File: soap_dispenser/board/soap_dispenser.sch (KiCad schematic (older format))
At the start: 43 parts, among them M1 Motor_DC, Q1 PMOS, Q11 NMOS, Q3 PMOS, Q4 NMOS, Q5 NMOS, SW1 SW_SPDT, SW8 SW_Push, U1 ATtiny48-AU

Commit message: Updated schema and capture files.
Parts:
- added C11, C18: C_Small, symbol Device:C_Small
- added RN7A, RN7B: 1M, symbol Device:R_Small_US
- added TP7: TestPoint, symbol Connector:TestPoint
- renumbered Q5 to Q2
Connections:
- net +6V: now also RN7A.1
- net CURRENT1: now also TP7.1
- net GNDD: now also C11.1, C18.1, RN7B.2
- net VSENSE: now reaches U1.19 (PA0)
- net VSENSE: now also J?.4 (Pin_4), C11.2, RN7A.2, RN7B.1
- net at Q?.2 (G), R23.2, R26.1: now also C18.2
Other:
- note added: "L-0"
- note added: "L-1"
- note added: "L-2"
- note added: "L-3"
- note added: "L-4"
- note added: "L-5"
- note added: "L-6"
- note added: "L-7"
- moved on the sheet: D4A, D4B, RN5A, RN5B, TP20, TP21

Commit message: Minor schema cleanup
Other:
- note added: "TODO: determine state of unconnected\npins (for minimal current)"
- moved on the sheet: C11, C?, D4A, D4B, R30, R9, RN5A, RN5B, RN6B?, RN7A, RN7B, SW1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

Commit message: First working version. Still a bunch of TODOs.
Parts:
- removed Q11, Q5, Q?: NMOS, symbol Device:Q_NMOS_DGS
- added Q11, Q5, Q?: MMBT4401, symbol Device:Q_NPN_BCE
- D4B: value YELLOW -> GREEN
- Q1, Q3: value PMOS -> DMG2305UX
- Q2, Q4: value NMOS -> DMG3420U
- renumbered C18 to C18_DNP
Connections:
- net CURRENT2: now also Q?.2 (C)
- net GNDD: now also Q11.3 (E), Q5.3 (E), Q?.3 (E)
- net at Q3.2 (G), RN6B.2: now also Q11.2 (C)
- net at Q1.2 (G), RN6A.2: now also Q5.2 (C)
- net at R5.1, R6.2: now also Q5.1 (B)
- net at R10.2, R10.2: now also Q11.1 (B)
- net at C18_DNP.2, R23.2, R26.1: now also Q?.1 (B)
- net #YELLOW renamed #GREEN
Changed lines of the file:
@@
 P 8350 2450
 F 0 "Q2" H 8556 2496 50  0000 L CNN
-F 1 "NMOS" H 7900 2600 50  0001 L CNN
+F 1 "DMG3420U" H 7900 2550 50  0000 L CNN
 F 2 "" H 8550 2550 50  0001 C CNN
 F 3 "~" H 8350 2450 50  0001 C CNN
@@
 P 6750 1550
 F 0 "Q3" H 6650 1400 50  0000 L CNN
-F 1 "PMOS" H 6950 1550 50  0001 L CNN
+F 1 "DMG2305UX" H 6950 1450 50  0000 L CNN
 F 2 "" H 6950 1650 50  0001 C CNN
 F 3 "~" H 6750 1550 50  0001 C CNN
@@
 	8550 1550 8750 1550
 $Comp
-L Device:Q_NMOS_DGS Q5
-U 1 1 5C0E3D5E
-P 8850 1800
-F 0 "Q5" H 9056 1846 50  0000 L CNN
-F 1 "NMOS" H 8400 1950 50  0001 L CNN
-F 2 "" H 9050 1900 50  0001 C CNN
-F 3 "~" H 8850 1800 50  0001 C CNN
-	1    8850 1800
-	-1   0    0    -1
-$EndComp
-$Comp
-L Device:Q_NMOS_DGS Q11
-U 1 1 5C0E41F9
-P 6250 1800
-F 0 "Q11" H 6456 1846 50  0000 L CNN
-F 1 "NMOS" H 6450 1750 50  0001 L CNN
-F 2 "" H 6450 1900 50  0001 C CNN
-F 3 "~" H 6250 1800 50  0001 C CNN
-	1    6250 1800
-	1    0    0    -1
-$EndComp
-$Comp
 L Device:R_Small_US R10
 U 1 1 5C0E4F52
@@
 P 8350 1550
 F 0 "Q1" H 8200 1400 50  0000 L CNN
-F 1 "PMOS" H 8556 1595 50  0001 L CNN
+F 1 "DMG2305UX" H 8500 1350 50  0000 L CNN
 F 2 "Package_TO_SOT_THT:TO-92_Inline" H 8550 1475 50  0001 L CIN
 F 3 "http://www.vishay.com/docs/70209/70209.pdf" H 8350 1550 50  0001 L CNN
@@
 U 1 1 5C0EEC8E
 P 6750 2450
-F 0 "Q4" H 6955 2450 50  0000 L CNN
-F 1 "NMOS" H 6955 2405 50  0001 L CNN
+F 0 "Q4" H 6950 2500 50  0000 L CNN
+F 1 "DMG3420U" H 6950 2400 50  0000 L CNN
 F 2 "" H 6950 2550 50  0001 C CNN
-F 3 "~" H 6750 2450 50  0001 C CNN
+F 3 "" H 6750 2450 50  0001 C CNN
 	1    6750 2450
 	1    0    0    -1
@@
 #RED
 Text GLabel 5050 5950 3    50   Input ~ 0
-#YELLOW
+#GREEN
 Text GLabel 2900 4650 2    50   Output ~ 0
 #RED
 Text GLabel 2900 4750 2    50   Output ~ 0
-#YELLOW
+#GREEN
 Wire Wire Line
 	2550 4650 2900 4650
@@
 P 5050 5300
 F 0 "D4B" V 5150 5200 50  0000 R CNN
-F 1 "YELLOW" V 5050 5200 50  0000 R CNN
+F 1 "GREEN" V 5050 5200 50  0000 R CNN
 F 2 "" H 5050 5300 50  0001 C CNN
 F 3 "~" H 5050 5300 50  0001 C CNN
@@
 	4150 7150 5650 7150
 $Comp
-L Device:Q_NMOS_DGS Q?
-U 1 1 5C1076F9
-P 8550 3600
-F 0 "Q?" H 8756 3646 50  0000 L CNN
-F 1 "NMOS" H 8100 3750 50  0001 L CNN
-F 2 "" H 8750 3700 50  0001 C CNN
-F 3 "~" H 8550 3600 50  0001 C CNN
-	1    8550 3600
-	1    0    0    -1
-$EndComp
-$Comp
 L Device:R_Small_US R19
 U 1 1 5C10B5B4
@@
 	7300 3600 7150 3600
 $Comp
-L Device:C_Small C18
+L Device:C_Small C18_DNP
 U 1 1 5C146FA6
 P 8000 3750
-F 0 "C18" H 7850 3850 50  0000 C CNN
+F 0 "C18_DNP" H 7800 3850 50  0000 C CNN
 F 1 "C_Small" V 8200 3800 50  0001 C CNN
 F 2 "" H 8000 3750 50  0001 C CNN
@@
 Wire Wire Line
 	8500 5300 8500 5400
+$Comp
+L Device:Q_NPN_BCE Q11
+U 1 1 5C137253
+P 6250 1800
+F 0 "Q11" H 6441 1846 50  0000 L CNN
+F 1 "MMBT4401" H 6441 1755 50  0000 L CNN
+F 2 "" H 6450 1900 50  0001 C CNN
+F 3 "~" H 6250 1800 50  0001 C CNN
+	1    6250 1800
+	1    0    0    -1
+$EndComp
+$Comp
+L Device:Q_NPN_BCE Q5
+U 1 1 5C1430B6
+P 8850 1800
+F 0 "Q5" H 9040 1846 50  0000 L CNN
+F 1 "MMBT4401" H 8500 2000 50  0000 L CNN
+F 2 "" H 9050 1900 50  0001 C CNN
+F 3 "" H 8850 1800 50  0001 C CNN
+	1    8850 1800
+	-1   0    0    -1
+$EndComp
+$Comp
+L Device:Q_NPN_BCE Q?
+U 1 1 5C155532
+P 8550 3600
+F 0 "Q?" H 8741 3646 50  0000 L CNN
+F 1 "MMBT4401" H 8741 3555 50  0000 L CNN
+F 2 "" H 8750 3700 50  0001 C CNN
+F 3 "~" H 8550 3600 50  0001 C CNN
+	1    8550 3600
+	1    0    0    -1
+$EndComp
 $EndSCHEMATC

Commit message: Added a comment with current sense resistor package size.
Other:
- note added: "SMD 1206\nAlso acting as \na fuse"
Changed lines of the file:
@@
 U 1 1 5C10B5B4
 P 7550 3050
-F 0 "R19" H 7600 3050 50  0000 L CNN
-F 1 "0R15" H 7600 3150 50  0000 L CNN
+F 0 "R19" H 7600 3000 50  0000 L CNN
+F 1 "0R15" H 7600 3100 50  0000 L CNN
 F 2 "" H 7550 3050 50  0001 C CNN
 F 3 "~" H 7550 3050 50  0001 C CNN
@@
 	1    0    0    -1
 $EndComp
+Text Notes 6650 3200 0    50   ~ 0
+SMD 1206\nAlso acting as \na fuse
 $EndSCHEMATC

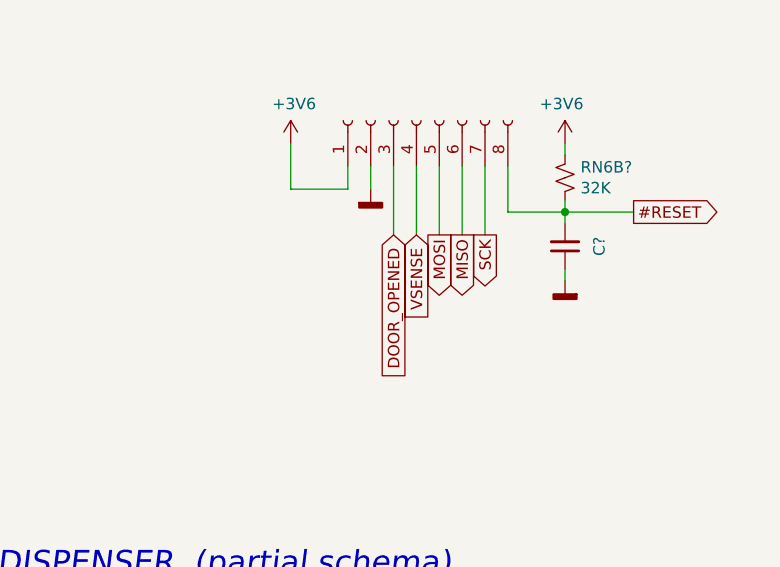
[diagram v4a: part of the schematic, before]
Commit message: Added sleep mode.
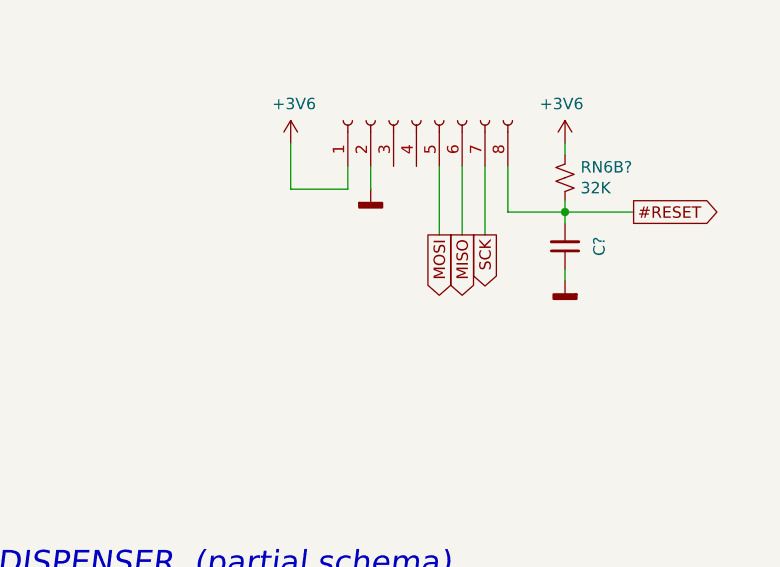
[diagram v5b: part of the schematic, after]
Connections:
- net DOOR_OPENED: no longer J?.3 (Pin_3)
- net VSENSE: no longer J?.4 (Pin_4)
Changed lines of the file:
@@
 Text GLabel 8900 5600 3    50   Output ~ 0
 MISO
-Wire Wire Line
-	8600 5300 8600 5600
 Text GLabel 8800 5600 3    50   Output ~ 0
 MOSI
-Text GLabel 8600 5600 3    50   Input ~ 0
-DOOR_OPENED
 Wire Wire Line
 	8900 5300 8900 5600
@@
 Wire Wire Line
 	2550 4050 2900 4050
-Text GLabel 8700 5600 3    50   Input ~ 0
-VSENSE
-Wire Wire Line
-	8700 5300 8700 5600
 $Comp
 L Connector:TestPoint TP7

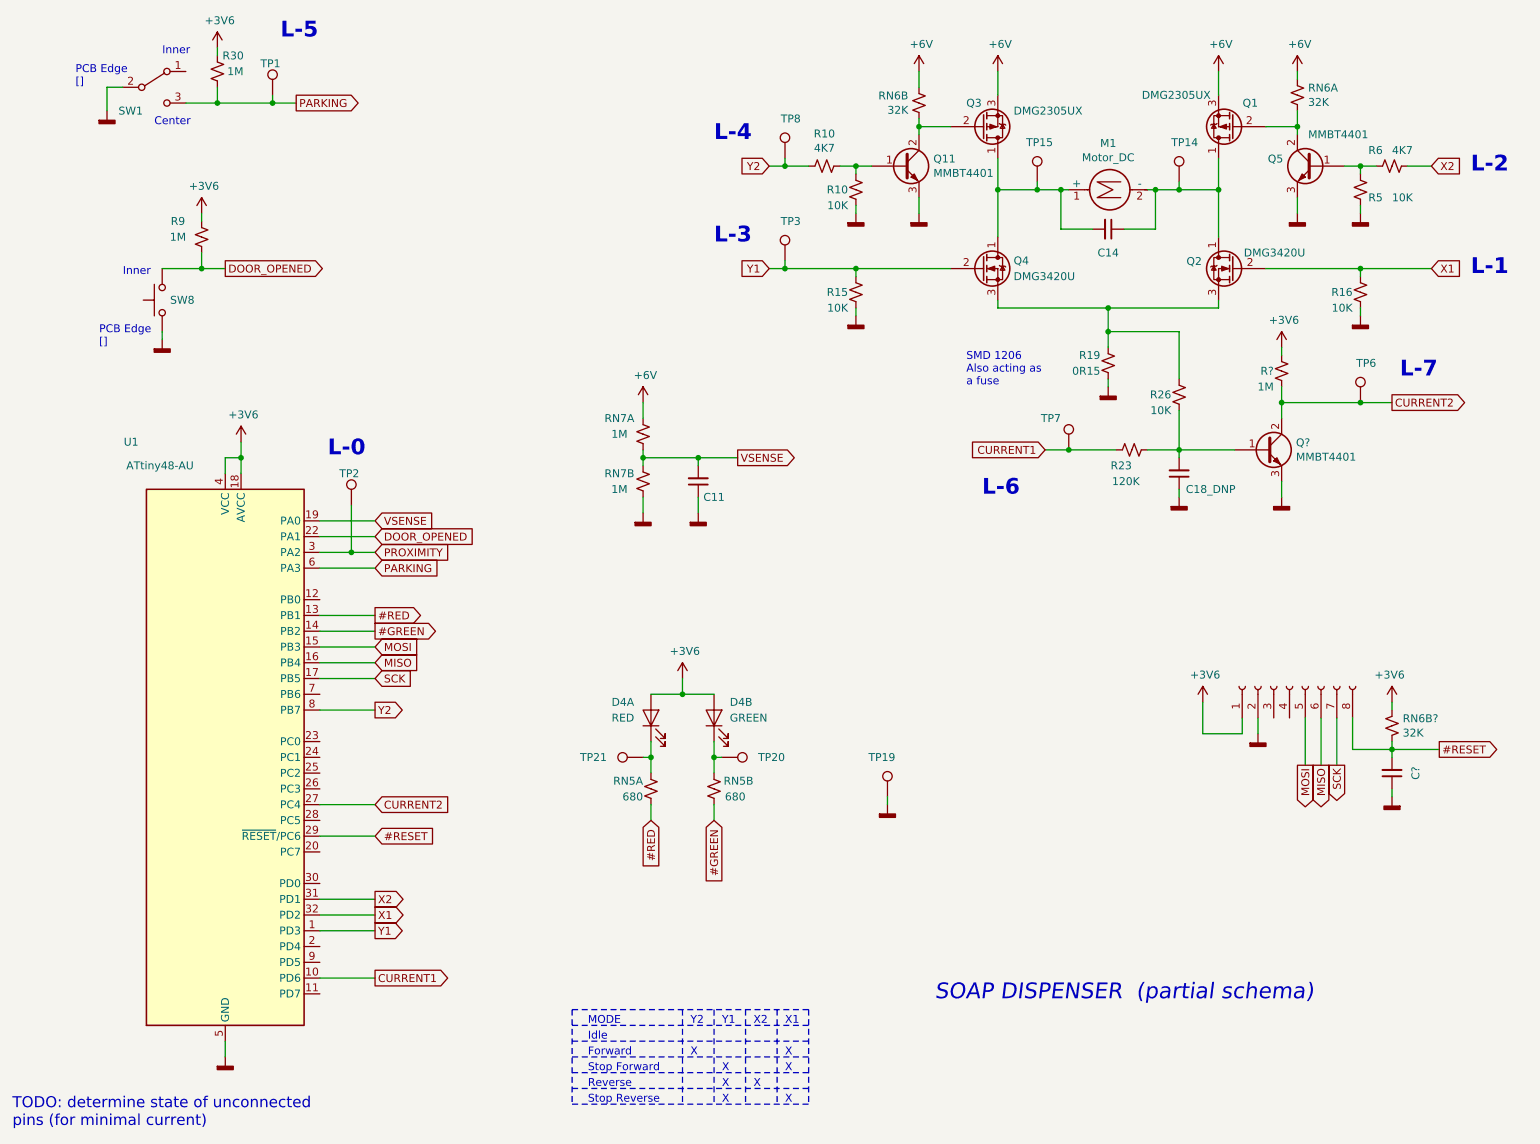
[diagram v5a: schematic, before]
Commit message: Changed the number of strokes per activation from 1 to two (more soap). Also minor cleanups.
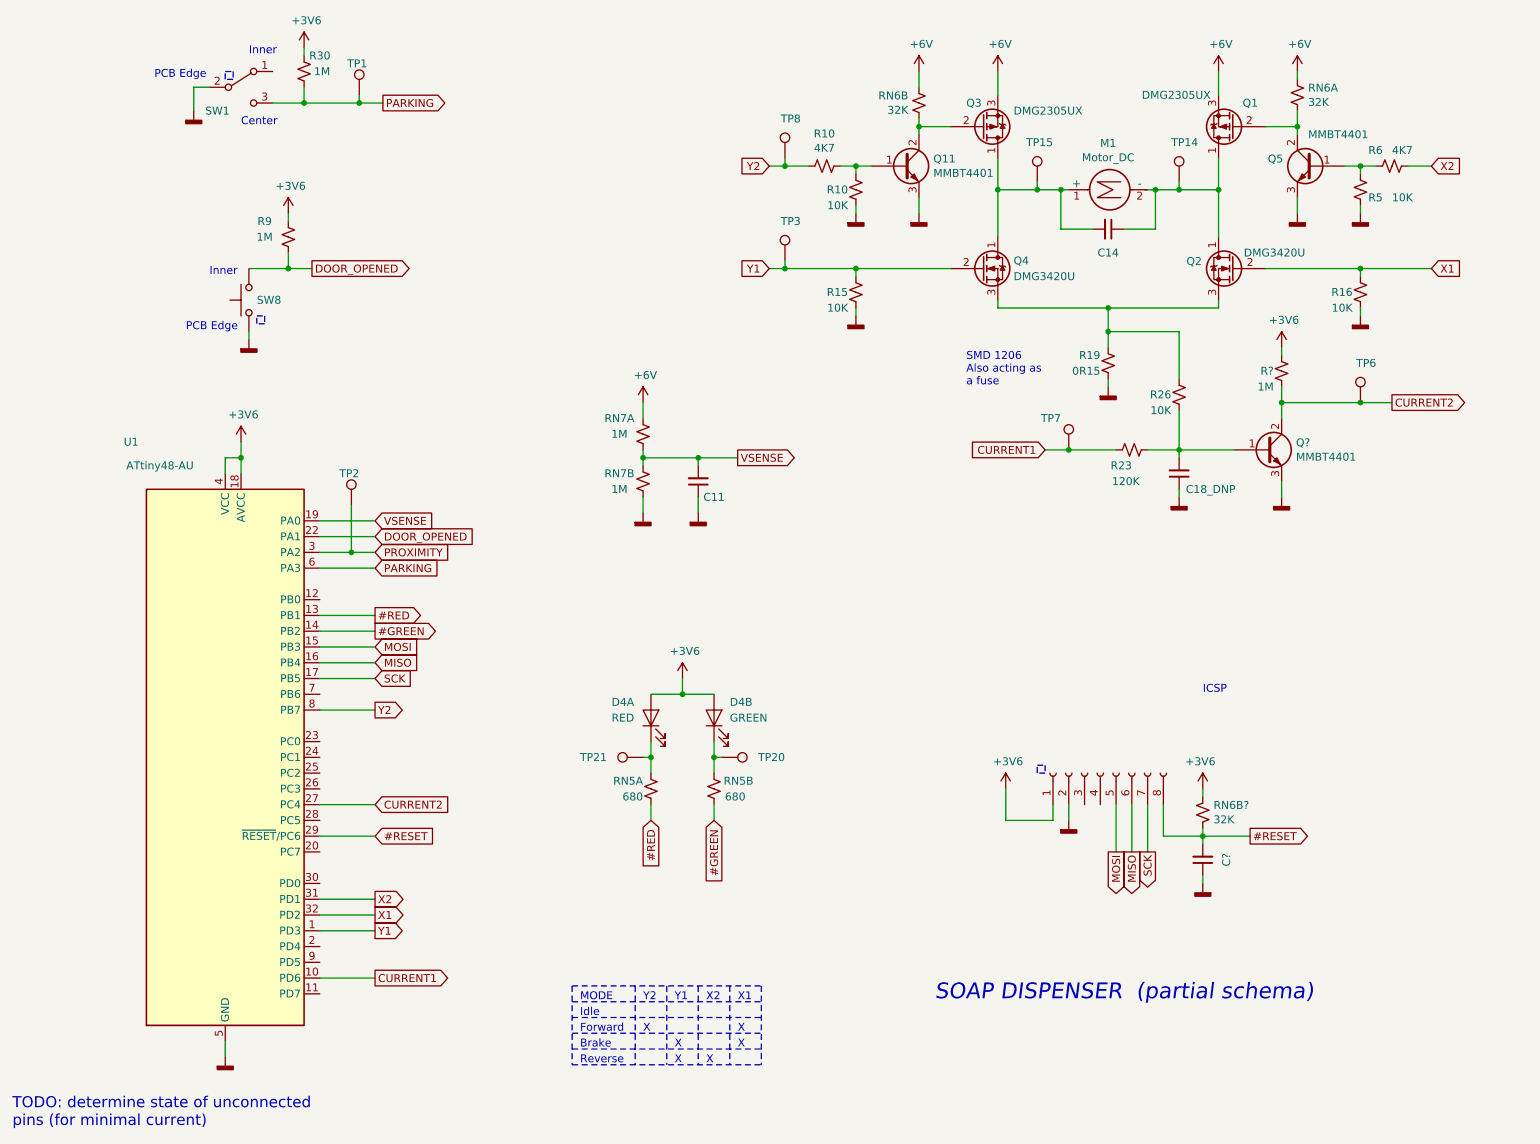
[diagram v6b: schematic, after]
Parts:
- removed TP19: TestPoint, symbol Connector:TestPoint
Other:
- note added: "Brake"
- note added: "ICSP"
- note added: "PCB Edge"
- note removed: "L-0"
- note removed: "L-1"
- note removed: "L-2"
- note removed: "L-3"
- note removed: "L-4"
- note removed: "L-5"
- note removed: "L-6"
- note removed: "L-7"
- note removed: "PCB Edge\n[]"
- note removed: "Stop Forward"
- note removed: "Stop Reverse"
- moved on the sheet: C?, R30, R9, RN6B?, SW1, SW8, TP1
